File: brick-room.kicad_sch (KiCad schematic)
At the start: 4 parts

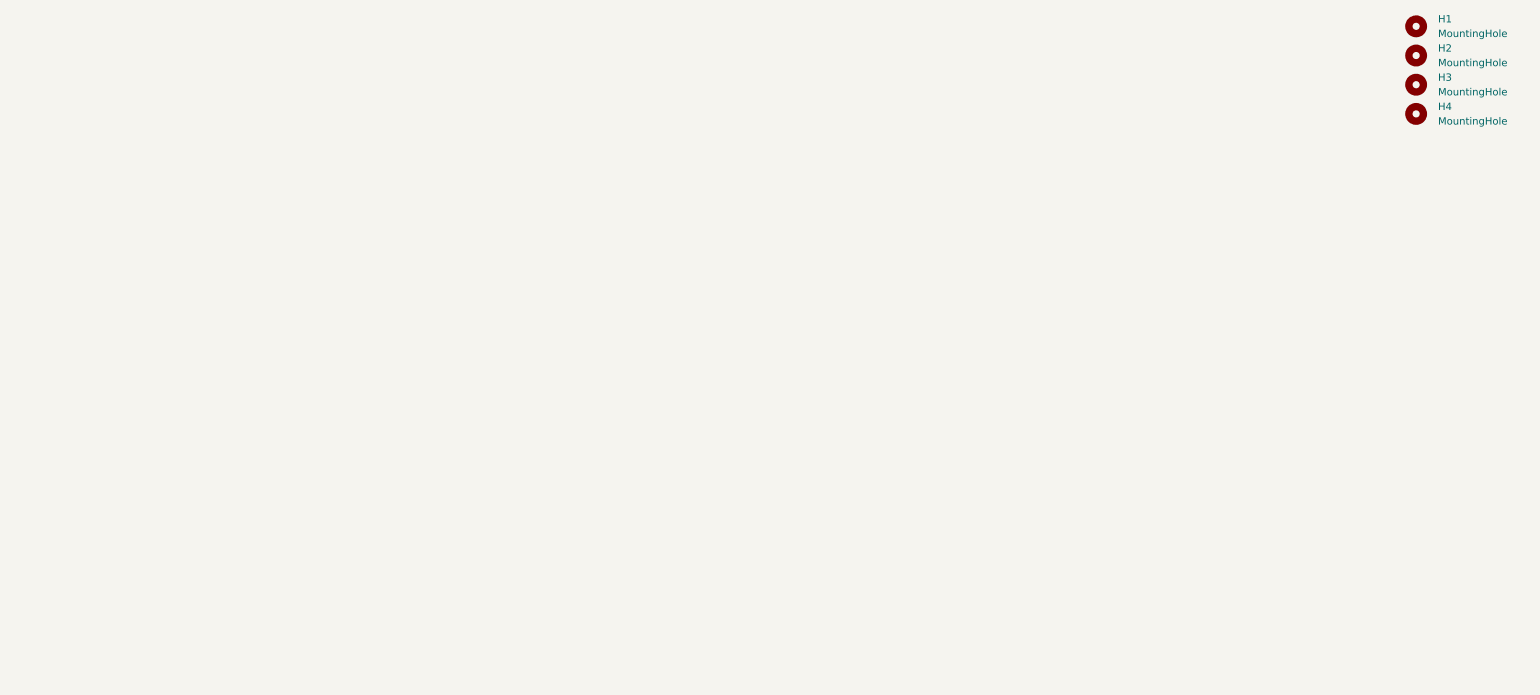
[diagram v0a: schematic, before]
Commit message: add power supply
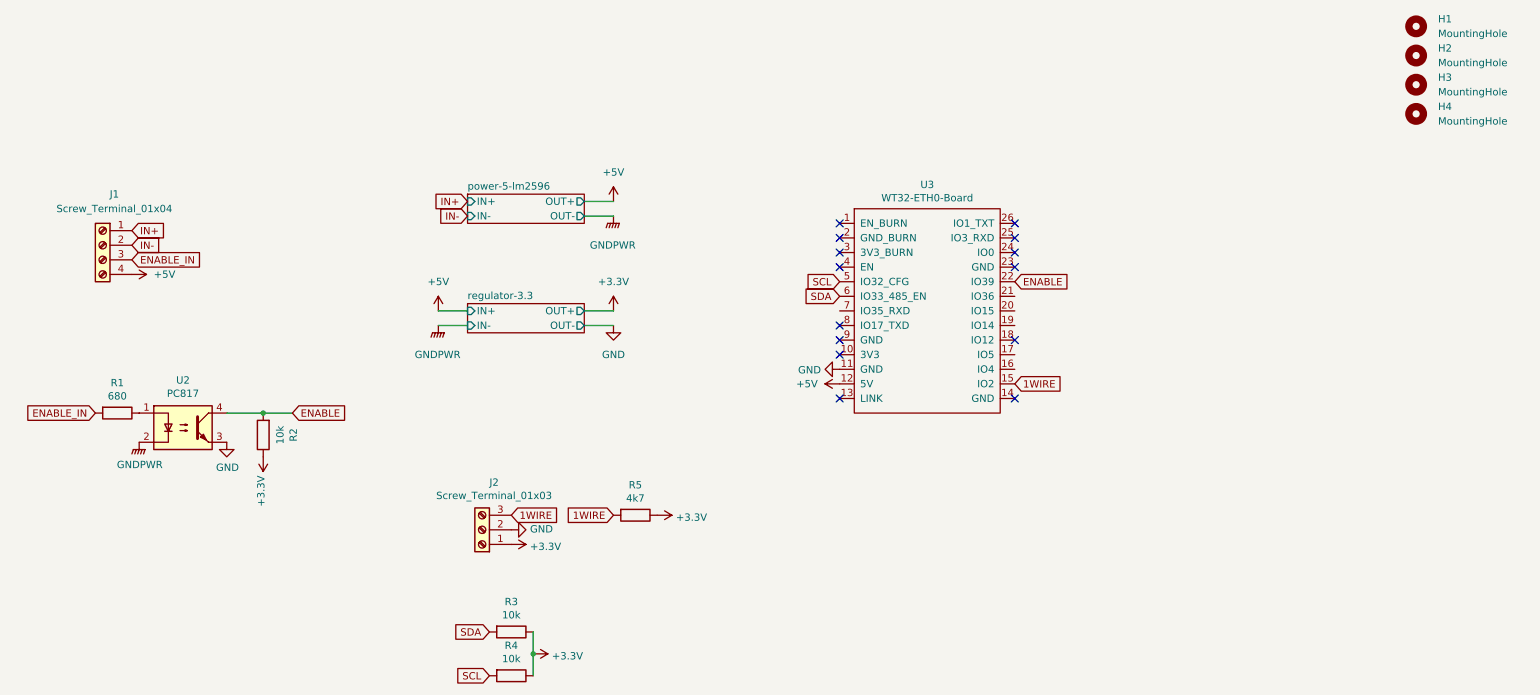
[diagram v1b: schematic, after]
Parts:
- added J1: Screw_Terminal_01x04, TerminalBlock:TerminalBlock_bornier-4_P5.08mm, symbol Connector:Screw_Terminal_01x04
- added J2: Screw_Terminal_01x03, TerminalBlock:TerminalBlock_bornier-3_P5.08mm, symbol Connector:Screw_Terminal_01x03
- added R1: 680, Resistor_THT:R_Axial_DIN0207_L6.3mm_D2.5mm_P7.62mm_Horizontal, symbol Device:R
- added R2, R3, R4: 10k, Resistor_THT:R_Axial_DIN0207_L6.3mm_D2.5mm_P7.62mm_Horizontal, symbol Device:R
- added R5: 4k7, Resistor_THT:R_Axial_DIN0207_L6.3mm_D2.5mm_P7.62mm_Horizontal, symbol Device:R
- added U2: PC817, Package_DIP:DIP-4_W7.62mm, symbol Isolator:PC817
- added U3: WT32-ETH0-Board, boards:WT32-ETH01-Board-Reversed, symbol master-wt32-eth01-rescue:WT32-ETH0-Board-boards
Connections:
- new net: R1.1, U2.1
- new net +3V3: J2.1 (Pin_1), R2.1, R3.1, R4.1, R5.1
- new net +5V: J1.4 (Pin_4), U3.12 (5V)
- new net 1WIRE: J2.3 (Pin_3), R5.2, U3.15 (IO2)
- new net ENABLE: R2.2, U2.4, U3.22 (IO39)
- new net ENABLE_IN: J1.3 (Pin_3), R1.2
- new net GND: J2.2 (Pin_2), U2.3, U3.11 (GND)
- new net GNDPWR: U2.2
- new net IN+: J1.1 (Pin_1)
- new net IN-: J1.2 (Pin_2)
- new net SCL: R4.2, U3.5 (IO32_CFG)
- new net SDA: R3.2, U3.6 (IO33_485_EN)
- no-connect marks 0 -> 14
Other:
- added sheet power-5-lm2596 (./include/power-lm2596.kicad_sch)
- added sheet regulator-3.3 (./include/regulator-3.3.kicad_sch)
